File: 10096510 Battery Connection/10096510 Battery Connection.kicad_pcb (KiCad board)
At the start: 2 copper layers, 68 x 45 mm, 42 parts, among them J1 09185107323, J3 811-S1-002-30-014101, J4 811-S1-002-30-014101, J5 811-S1-002-30-014101, J6 GKS-913-0024

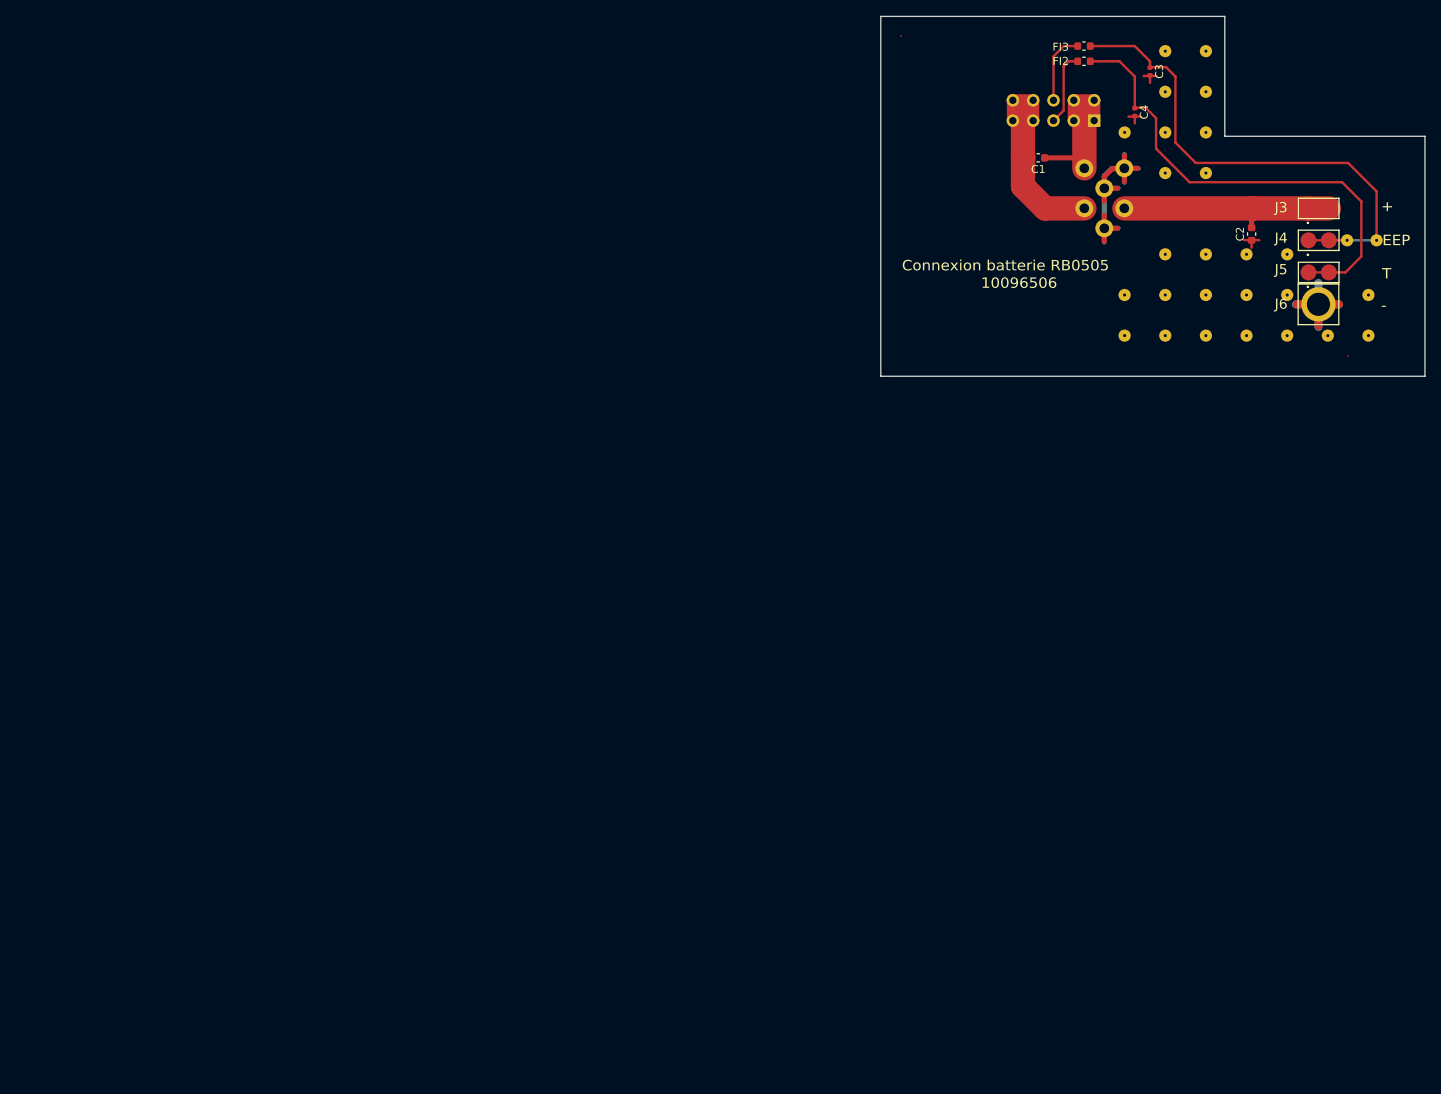
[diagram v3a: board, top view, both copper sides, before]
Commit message: WIP. Merged the layout conversion info from George. Updated library footprint pads for filter and through-hole connectors per the layout conversion info. Added gnd planes and sitching vias. Added assembly and fabrication notes.
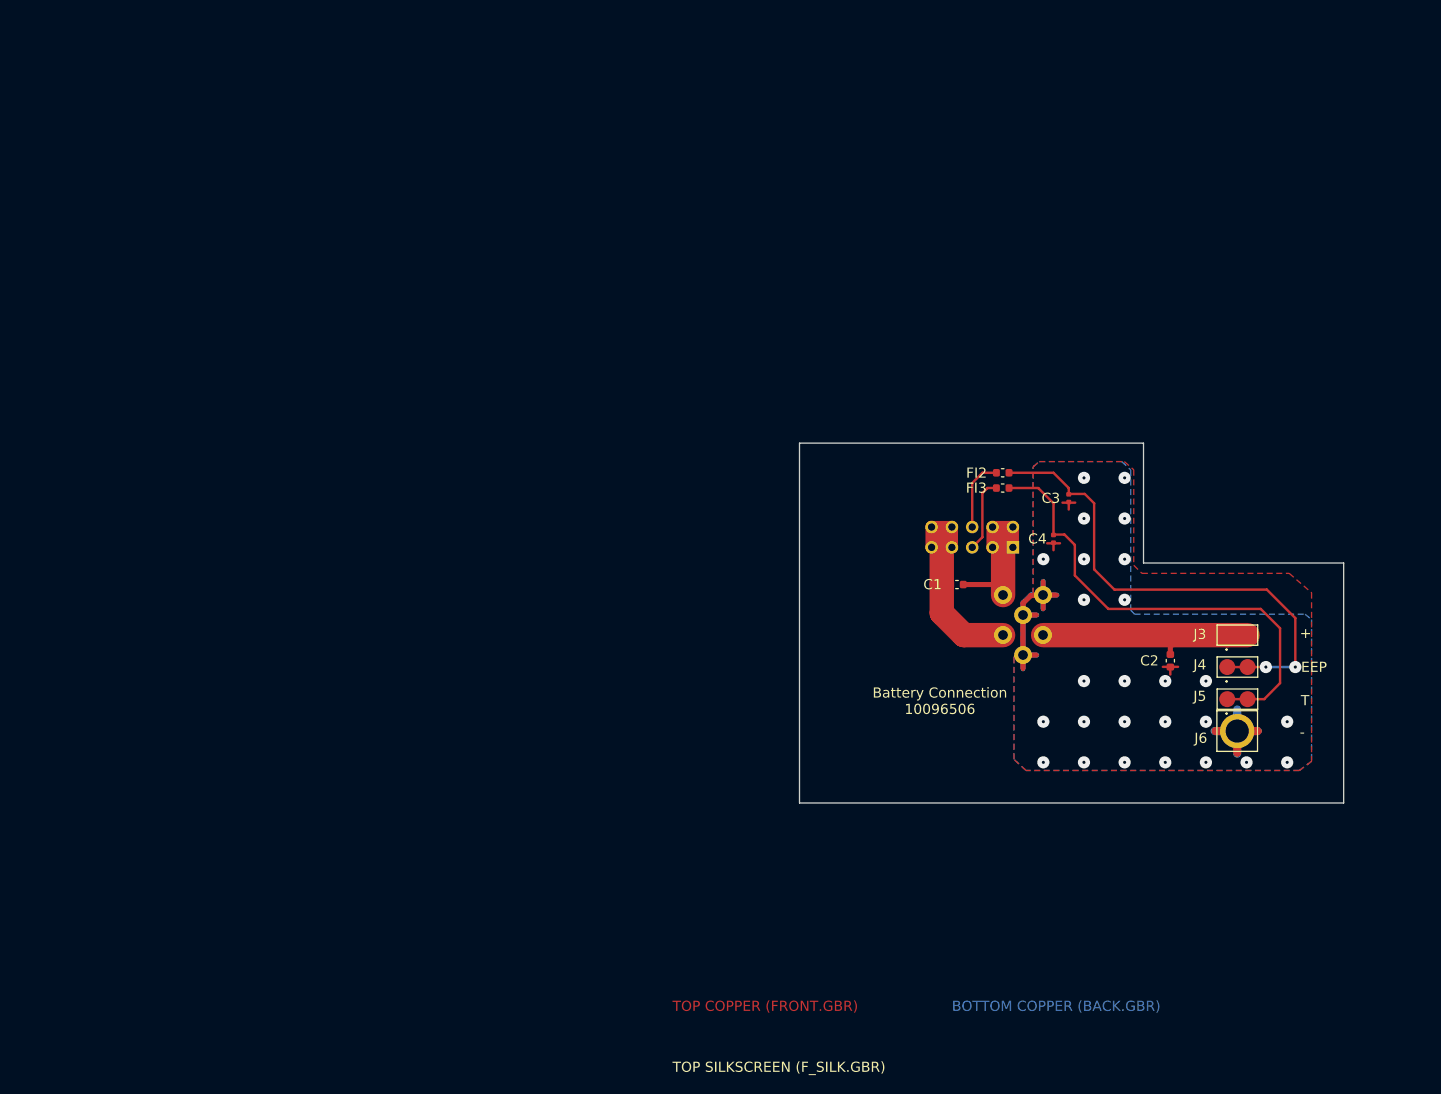
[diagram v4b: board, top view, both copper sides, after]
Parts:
- removed ? (x28): , 
- removed PT1, PT2: MIRECMS, MIRECMS_D-1.5_1
- moved J6 54.3 mm to (248.1, 133.1)
- moved C2 54.3 mm to (239.8, 124.3)
- moved FI1 54.3 mm to (221.4, 118.6)
- moved FI3 54.3 mm to (218.8, 102.8)
- moved J3 54.3 mm to (248.2, 121.1)
- moved C1 54.3 mm to (213.1, 114.8)
- moved C3 54.3 mm to (227.1, 104.0)
- moved C4 54.3 mm to (225.2, 109.1)
- moved FI2 54.3 mm to (218.8, 100.8)
- moved J1 54.3 mm to (220.1, 110.2)
- moved J4 54.3 mm to (248.2, 125.1)
- moved J5 54.3 mm to (248.2, 129.1)
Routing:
- net GND: track 90.5 -> 92.1 mm, vias 0 -> 26
- net /BAT_EEPROM: vias 0 -> 2
- added copper zone on B.Cu, net GND
- added copper zone on F.Cu, net GND
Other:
- board text added: "ASSEMBLY NOTES ------------------------------------------------------------ 1. MANUFACTURE ACCORDING IPC A610 CLASS III 2. ALL FABRICATION PROCESSES TO BE ROHS COMPLIANT. 3. MARK BOARD PER J-STD-609A 4. LEVEL OFF PINS OF FI1 FILTER TO WITHIN 1.4MM FROM PCB SURFACE. 5. WARNING : EXCESSIVE TEMPERATURE COULD DESTROY THE J6 CONNECTOR SPRING."
- board text added: "BOTTOM COPPER (BACK.GBR)"
- board text added: "BOTTOM PASTEMASK (B_PASTE.GBR)"
- board text added: "BOTTOM SILKSCREEN (B_SILK.GBR)"
- board text added: "BOTTOM SOLDERMASK (B_MASK.GBR)"
- board text added: "Battery Connection 10096506"
- board text added: "FABRICATION NOTES ------------------------------------------------------------ 1. MANUFACTURE ACCORDING IPC A610 CLASS III 2. MATERIAL : COPPER CLAD LAMINATES ISOLA 370HR (OR EQUIVALENT), ROHS COMPLIANT. U.L. DESIGNATION : ANSI GRADE FR4 PER IPC 4101. 3. FINISH ; ALL EXPOSED CONDUCTIVE SURFACES TO ELECTROLESS NICKEL IMMERSION GOLD (ENIG) PLATED USING 100-400 MICROINCHES NICKEL AND 3-8 MICROINCHES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"
- board text added: "TOP COPPER (FRONT.GBR)"
- board text added: "TOP PASTEMASK (F_PASTE.GBR)"
- board text added: "TOP SILKSCREEN (F_SILK.GBR)"
- board text added: "TOP SOLDERMASK (F_MASK.GBR)"
- board text removed: "0,4"
- board text removed: "0,9"
- board text removed: "1,2"
- board text removed: "10096506"
- board text removed: "2,9"
- board text removed: "ATTENTION: WARNING:"
- board text removed: "Connexion batterie RB0505"
- board text removed: "Fabrique suivant IPC A610 classe III. Manufactured according to IPC A610 class III."
- board text removed: "Le circuit imprime doit etre UL94V-0. The printed circuit board must be UL94V-0. Le fabricant doit etre reconnu UL et doit apposer le marquage correspondant. The manufacturer must be recognized UL and must affix corresponding marking."

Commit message: WIP - Working to address library syncing.
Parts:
- C1, C2: footprint 10096510 Battery Connection:C_0603_1608Metric -> 10096510_Battery_Connection:C_0603_1608Metric
- C3, C4: footprint 10096510 Battery Connection:C_0402_1005Metric -> 10096510_Battery_Connection:C_0402_1005Metric
- FI1: footprint 10096510 Battery Connection:BNX002-011 -> 10096510_Battery_Connection:BNX002-011
- FI2, FI3: footprint 10096510 Battery Connection:L_0603_1608Metric -> 10096510_Battery_Connection:L_0603_1608Metric
- J1: footprint 10096510 Battery Connection:SHDRRA10W64P254_2X5_2050X890X930P -> 10096510_Battery_Connection:SHDRRA10W64P254_2X5_2050X890X930P
- J3, J4, J5: footprint 10096510 Battery Connection:CONN_811S100230014101 -> 10096510_Battery_Connection:CONN_811S100230014101
- J6: footprint 10096510 Battery Connection:CONN_GKS-913-Z -> 10096510_Battery_Connection:CONN_GKS-913-Z

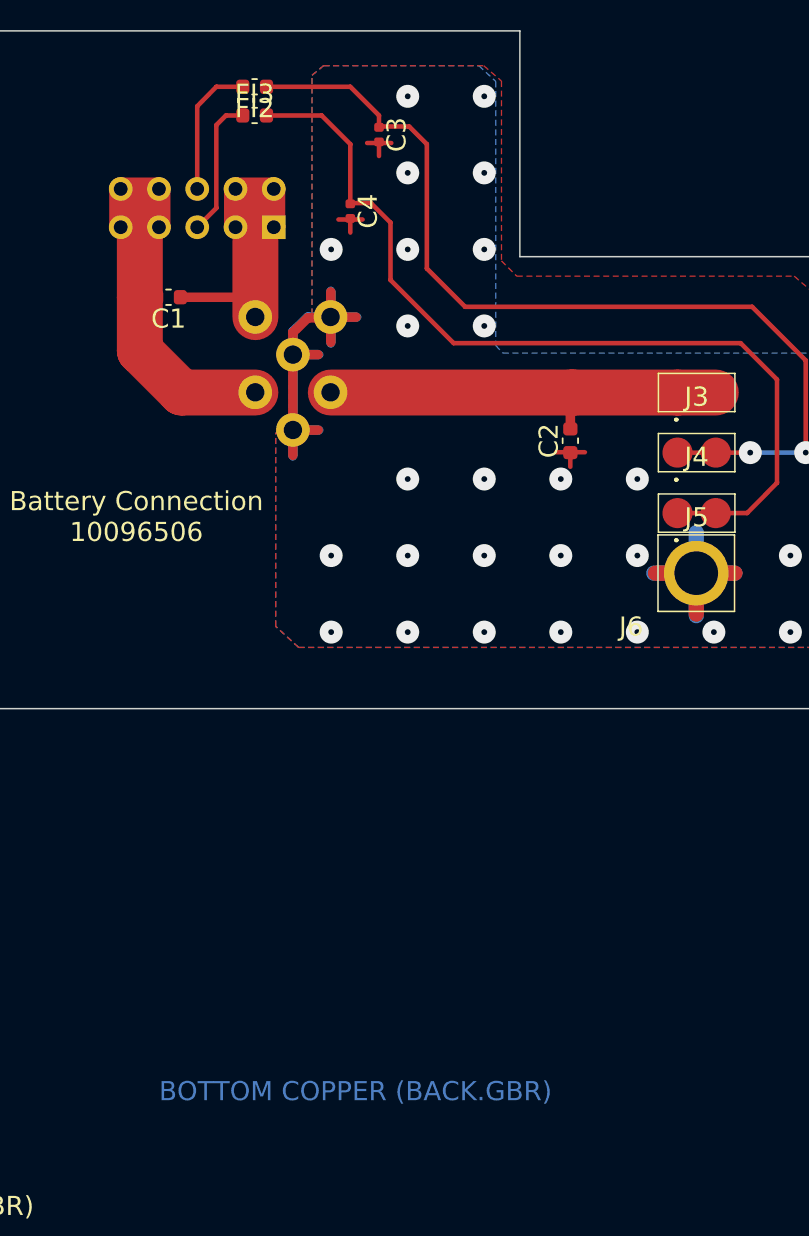
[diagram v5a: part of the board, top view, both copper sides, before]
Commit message: Added keepout regions for mounting purposes, and fabrication note regarding trace label.
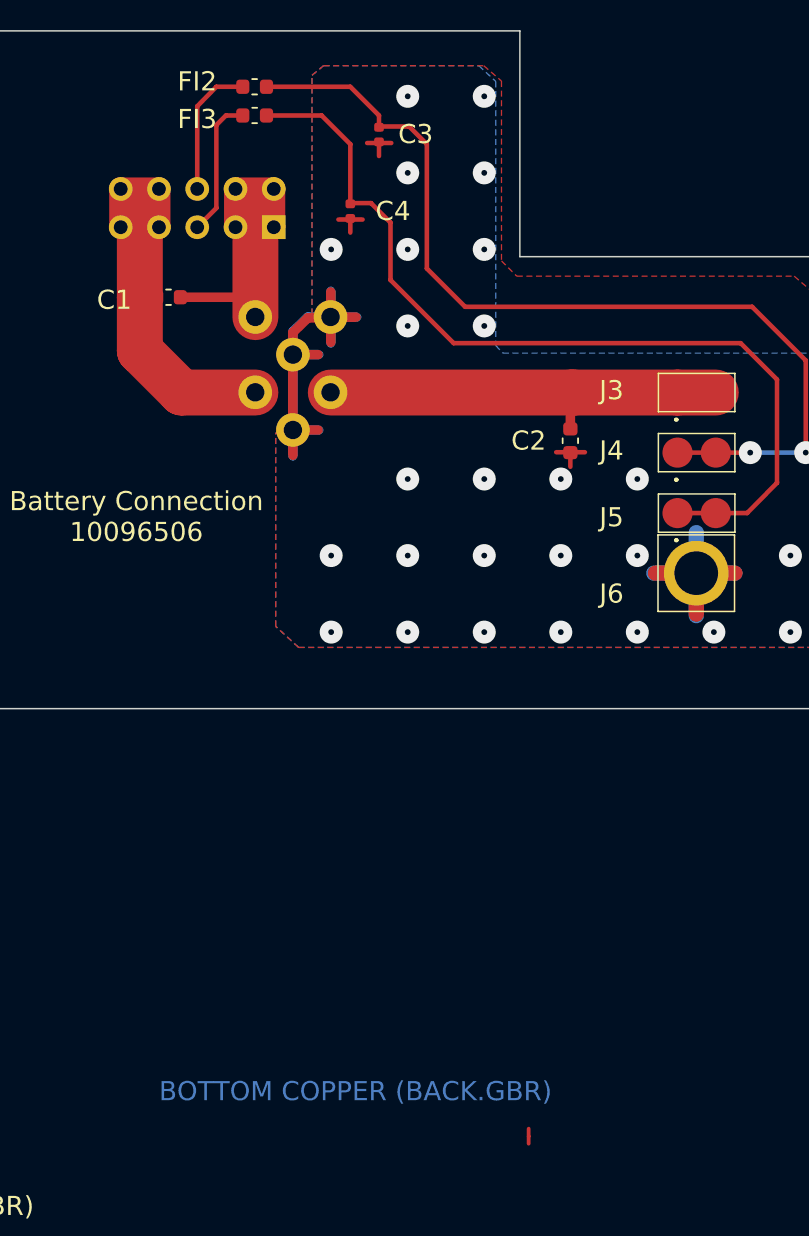
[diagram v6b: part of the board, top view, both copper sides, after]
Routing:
- net (no net): track 0.00 -> 1.00 mm
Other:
- board text added: "ASSEMBLY NOTES ------------------------------------------------------------ 1. MANUFACTURE ACCORDING IPC A610 CLASS III 2. ALL FABRICATION PROCESSES TO BE ROHS COMPLIANT. 3. MARK BOARD PER J-STD-609A 4. LEVEL OFF PINS OF FI1 FILTER TO WITHIN 1.4MM FROM PCB SURFACE. 5. WARNING : EXCESSIVE TEMPERATURE COULD DESTROY THE J6 CONNECTOR SPRING. 6. PLACE TRACEABILITY LABEL ON BOTTOM SIDE IN REGION MARKED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"
- board text removed: "ASSEMBLY NOTES ------------------------------------------------------------ 1. MANUFACTURE ACCORDING IPC A610 CLASS III 2. ALL FABRICATION PROCESSES TO BE ROHS COMPLIANT. 3. MARK BOARD PER J-STD-609A 4. LEVEL OFF PINS OF FI1 FILTER TO WITHIN 1.4MM FROM PCB SURFACE. 5. WARNING : EXCESSIVE TEMPERATURE COULD DESTROY THE J6 CONNECTOR SPRING."
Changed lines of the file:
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@@
     (thickness 1.6)
     (drawings 102)
-    (tracks 138)
+    (tracks 140)
     (zones 0)
     (modules 12)
@@
   (page A4)
   (layers
-    (0 F.Cu signal)
+    (0 F.Cu signal hide)
     (31 B.Cu signal)
     (32 B.Adhes user)
     (33 F.Adhes user)
-    (34 B.Paste user)
+    (34 B.Paste user hide)
     (35 F.Paste user)
-    (36 B.SilkS user)
+    (36 B.SilkS user hide)
     (37 F.SilkS user)
     (38 B.Mask user)
@@
     (solder_mask_min_width 0.25)
     (aux_axis_origin 0 0)
-    (grid_origin 134.9932 137.043)
     (visible_elements 7FFFFF7F)
     (pcbplotparams
@@
     (tags Connector)
     (attr smd)
-    (fp_text reference J6 (at -4.318 3.556) (layer F.SilkS)
+    (fp_text reference J6 (at -5.6248 1.3686) (layer F.SilkS)
       (effects (font (size 1.27 1.27) (thickness 0.254)))
     )
@@
     (tags Connector)
     (attr smd)
-    (fp_text reference J5 (at 0 0.29) (layer F.SilkS)
+    (fp_text reference J5 (at -5.6502 0.29) (layer F.SilkS)
       (effects (font (size 1.27 1.27) (thickness 0.254)))
     )
@@
     (tags Connector)
     (attr smd)
-    (fp_text reference J4 (at 0 0.29) (layer F.SilkS)
+    (fp_text reference J4 (at -5.6502 -0.1304) (layer F.SilkS)
       (effects (font (size 1.27 1.27) (thickness 0.254)))
     )
@@
     (tags Connector)
     (attr smd)
-    (fp_text reference J3 (at 0 0.29) (layer F.SilkS)
+    (fp_text reference J3 (at -5.6502 -0.1426) (layer F.SilkS)
       (effects (font (size 1.27 1.27) (thickness 0.254)))
     )
@@
     (tags inductor)
     (attr smd)
-    (fp_text reference FI3 (at 0 -1.43) (layer F.SilkS)
+    (fp_text reference FI3 (at -3.8132 0.247) (layer F.SilkS)
       (effects (font (size 1.27 1.27) (thickness 0.254)))
     )
@@
     (tags inductor)
     (attr smd)
-    (fp_text reference FI2 (at 0 -1.43) (layer F.SilkS)
+    (fp_text reference FI2 (at 3.8132 0.348) (layer F.SilkS)
       (effects (font (size 1.27 1.27) (thickness 0.254)))
     )
@@
     (tags capacitor)
     (attr smd)
-    (fp_text reference C4 (at 0 -1.17 90) (layer F.SilkS)
+    (fp_text reference C4 (at 0 -2.8368) (layer F.SilkS)
       (effects (font (size 1.27 1.27) (thickness 0.254)))
     )
@@
     (tags capacitor)
     (attr smd)
-    (fp_text reference C3 (at 0 -1.17 90) (layer F.SilkS)
+    (fp_text reference C3 (at -0.023 -2.4318) (layer F.SilkS)
       (effects (font (size 1.27 1.27) (thickness 0.254)))
     )
@@
     (tags capacitor)
     (attr smd)
-    (fp_text reference C2 (at 0 -1.43 90) (layer F.SilkS)
+    (fp_text reference C2 (at 0 -2.7682) (layer F.SilkS)
       (effects (font (size 1.27 1.27) (thickness 0.254)))
     )
@@
     (tags capacitor)
     (attr smd)
-    (fp_text reference C1 (at 0 -1.43) (layer F.SilkS)
+    (fp_text reference C1 (at 3.5982 -0.182) (layer F.SilkS)
       (effects (font (size 1.27 1.27) (thickness 0.254)))
     )
@@
   )
   (dimension 29.9974 (width 0.1524) (layer Eco2.User)
-    (gr_text "29.997 mm" (at 273.474 127.1243 90) (layer Eco2.User)
+    (gr_text "30 mm" (at 273.474 127.1243 90) (layer Eco2.User)
       (effects (font (size 1.016 1.016) (thickness 0.1524)))
     )
@@
   )
   (dimension 68.0212 (width 0.1524) (layer Eco2.User)
-    (gr_text "68.021 mm" (at 227.4238 156.1438) (layer Eco2.User)
+    (gr_text "68 mm" (at 227.4238 156.1438) (layer Eco2.User)
       (effects (font (size 1.016 1.016) (thickness 0.1524)))
     )
@@
   )
   (dimension 44.9834 (width 0.1524) (layer Eco2.User)
-    (gr_text "44.983 mm" (at 179.392401 119.6313 270) (layer Eco2.User)
+    (gr_text "45 mm" (at 179.392401 119.6313 270) (layer Eco2.User)
       (effects (font (size 1.016 1.016) (thickness 0.1524)))
     )
@@
     (arrow2b (pts (xy 180.713201 97.1396) (xy 181.299622 98.266104)))
   )
-  (gr_text "ASSEMBLY NOTES\n------------------------------------------------------------\n\n1. MANUFACTURE ACCORDING IPC A610 CLASS III\n\n2. ALL FABRICATION PROCESSES TO BE ROHS COMPLIANT.\n\n3. MARK BOARD PER J-STD-609A\n\n4. LEVEL OFF PINS OF FI1 FILTER TO WITHIN 1.4MM FROM PCB SURFACE.\n\n5. WARNING : EXCESSIVE TEMPERATURE COULD DESTROY THE J6 CONNECTOR SPRING." (at 31.8692 124.343) (layer Eco2.User)
+  (gr_text "ASSEMBLY NOTES\n------------------------------------------------------------\n\n1. MANUFACTURE ACCORDING IPC A610 CLASS III\n\n2. ALL FABRICATION PROCESSES TO BE ROHS COMPLIANT.\n\n3. MARK BOARD PER J-STD-609A\n\n4. LEVEL OFF PINS OF FI1 FILTER TO WITHIN 1.4MM FROM PCB SURFACE.\n\n5. WARNING : EXCESSIVE TEMPERATURE COULD DESTROY THE J6 CONNECTOR SPRING.\n\n6. PLACE TRACEABILITY LABEL ON BOTTOM SIDE IN REGION MARKED BY SILLK." (at 31.8692 124.343) (layer Eco2.User)
     (effects (font (size 1.27 1.27) (thickness 0.254)) (justify left))
   )
@@
   (gr_line (start 193.4132 97.1396) (end 236.4154 97.1396) (layer Dwgs.User) (width 0.0762))
   (gr_line (start 236.4154 112.1256) (end 236.4154 97.1396) (layer Dwgs.User) (width 0.0762))
+  (segment (start 237 171) (end 237 170.5) (width 0.25) (layer F.Cu) (net 0))
+  (segment (start 237 170.5) (end 237 170) (width 0.25) (layer F.Cu) (net 0))
   (segment (start 213.9618 121.1426) (end 218.864 121.1426) (width 3.048) (layer F.Cu) (net 1))
   (segment (start 211.1932 118.374) (end 213.9618 121.1426) (width 3.048) (layer F.Cu) (net 1))
@@
       )
     )
+  )
+  (zone (net 0) (net_name "") (layers F&B.Cu) (hatch edge 0.508)
+    (connect_pads (clearance 0.508))
+    (min_thickness 0.254)
+    (keepout (tracks not_allowed) (vias not_allowed) (copperpour allowed))
+    (fill (arc_segments 32) (thermal_gap 0.508) (thermal_bridge_width 0.508))
+    (polygon
+      (pts
+        (xy 261.4344 142.123) (xy 257.4344 142.123) (xy 257.4344 133.623) (xy 261.4344 133.623)
+      )
+    )
+  )
+  (zone (net 0) (net_name "") (layers F&B.Cu) (hatch edge 0.508)
+    (connect_pads (clearance 0.508))
+    (min_thickness 0.254)
+    (keepout (tracks not_allowed) (vias not_allowed) (copperpour allowed))
+    (fill (arc_segments 32) (thermal_gap 0.508) (thermal_bridge_width 0.508))
+    (polygon
+      (pts
+        (xy 193.4132 142.123) (xy 197.4132 142.123) (xy 197.4132 133.623) (xy 193.4132 133.623)
+      )
+    )
+  )
+  (zone (net 0) (net_name "") (layer B.Cu) (hatch edge 0.508)
+    (connect_pads (clearance 0.508))
+    (min_thickness 0.254)
+    (keepout (tracks not_allowed) (vias not_allowed) (copperpour not_allowed))
+    (fill (arc_segments 32) (thermal_gap 0.508) (thermal_bridge_width 0.508))
+    (polygon
+      (pts
+        (xy 254.4344 118.123) (xy 241.9344 118.123) (xy 241.9344 112.123) (xy 254.4344 112.123)
+      )
+    )
